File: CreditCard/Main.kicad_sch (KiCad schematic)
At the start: 0 parts

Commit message: début
début sch
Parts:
- added C10, C11, C18, C19, C20, C21: 0.1uF, Capacitor_SMD:C_0603_1608Metric, symbol Device:C
- added SW1, SW2, SW3: 2425754-1, Library:2425754-1_TEC, symbol LIB:2425754-1
- added U5, U6, U7: PTS645SK43SMTR92LFS, Library:SWITCH_45SK43SMTR92LFS, symbol Library:PTS645SK43SMTR92LFS
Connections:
- new net GND: C10.2, C11.2, C18.2, C19.2, C20.2, C21.2, SW1.2, SW1.3, SW2.2, SW2.3, SW3.2, SW3.3, U5.3, U5.4, U6.3, U6.4, U7.3, U7.4
- new net GPIO2: C10.1, SW1.1, SW1.4
- new net GPIO3: C11.1, SW2.1, SW2.4
- new net GPIO4: C18.1, SW3.1, SW3.4
- new net GPIO5: C19.1, U5.1, U5.2
- new net GPIO6: C20.1, U6.1, U6.2
- new net GPIO7: C21.1, U7.1, U7.2
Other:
- note added: "JEUX"
- note added: "MENU"

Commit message: manque écran
manque seulement l'écran le reste est ajouter
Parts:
- added U10: PAM8403DR, Library:SOIC_8403DR_DIO, symbol Library:PAM8403DR
- added U9: SPKM.36.8.B, Library:SPEAKER, symbol Library:SPEAKER
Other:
- note added: "SPEAKER"
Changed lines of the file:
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@@
 		)
 	)
+	(rectangle
+		(start 129.54 15.24)
+		(end 241.3 93.98)
+		(stroke
+			(width 0.381)
+			(type dash)
+			(color 20 0 0 1)
+		)
+		(fill
+			(type none)
+		)
+	)
 	(text "JEUX\n"
 		(exclude_from_sim no)
@@
 		)
 	)
+	(text "SPEAKER\n"
+		(exclude_from_sim no)
+		(at 138.43 19.812 0)
+		(effects
+			(font
+				(size 2.286 2.286)
+				(thickness 0.4064)
+				(bold yes)
+			)
+		)
+	)
 	(text "MENU"
 		(exclude_from_sim no)
@@
 	)
 	(symbol
+		(lib_id "Library:SPEAKER")
+		(at 214.63 48.26 0)
+		(unit 1)
+		(exclude_from_sim no)
+		(in_bom yes)
+		(on_board yes)
+		(dnp no)
+		(fields_autoplaced yes)
+		(property "Reference" "U9"
+			(at 219.075 41.91 0)
+			(effects
+				(font
+					(size 1.27 1.27)
+				)
+			)
+		)
+		(property "Value" "SPKM.36.8.B"
+			(at 219.075 44.45 0)
+			(effects
+				(font
+					(size 1.27 1.27)
+				)
+			)
+		)
+		(property "Footprint" "Library:SPEAKER"
+			(at 214.63 48.26 0)
+			(effects
+				(font
+					(size 1.27 1.27)
+				)
+				(hide yes)
+			)
+		)
+		(property "Datasheet" "https://www.taoglas.com/datasheets/SPKM.36.8.B.pdf"
+			(at 214.63 48.26 0)
+			(effects
+				(font
+					(size 1.27 1.27)
+				)
+				(hide yes)
+			)
+		)
+		(property "Description" ""
+			(at 214.63 48.26 0)
+			(effects
+				(font
+					(size 1.27 1.27)
+				)
+				(hide yes)
+			)
+		)
+		(pin "2"
+		)
+		(pin "1"
+		)
+		(instances
+			(project ""
+				(path "/374dba13-75d6-44a0-b8b2-0ca0aa70330e/712f9979-8db9-4af3-ac95-adf708c06b03"
+					(reference "U9")
+					(unit 1)
+				)
+			)
+		)
+	)
+	(symbol
 		(lib_id "Device:C")
 		(at 74.93 53.34 0)
@@
 					(unit 1)
 				)
+			)
+		)
+	)
+	(symbol
+		(lib_id "Library:PAM8403DR")
+		(at 137.16 44.45 0)
+		(unit 1)
+		(exclude_from_sim no)
+		(in_bom yes)
+		(on_board yes)
+		(dnp no)
+		(fields_autoplaced yes)
+		(property "Reference" "U10"
+			(at 162.56 34.29 0)
+			(effects
+				(font
+					(size 1.524 1.524)
+				)
+			)
+		)
+		(property "Value" "PAM8403DR"
+			(at 162.56 36.83 0)
+			(effects
+				(font
+					(size 1.524 1.524)
+				)
+			)
+		)
+		(property "Footprint" "Library:SOIC_8403DR_DIO"
+			(at 137.16 44.45 0)
+			(effects
+				(font
+					(size 1.27 1.27)
+					(italic yes)
+				)
+				(hide yes)
+			)
+		)
+		(property "Datasheet" "PAM8403DR"
+			(at 137.16 44.45 0)
+			(effects
+				(font
+					(size 1.27 1.27)
+					(italic yes)
+				)
+				(hide yes)
+			)
+		)
+		(property "Description" ""
+			(at 137.16 44.45 0)
+			(effects
+				(font
+					(size 1.27 1.27)
+				)
+				(hide yes)
+			)
+		)
+		(pin "1"
+		)
+		(pin "3"
+		)
+		(pin "2"
+		)
+		(pin "7"
+		)
+		(pin "8"
+		)
+		(pin "4"
+		)
+		(pin "16"
+		)
+		(pin "13"
+		)
+		(pin "11"
+		)
+		(pin "6"
+		)
+		(pin "14"
+		)
+		(pin "10"
+		)
+		(pin "12"
+		)
+		(pin "5"
+		)
+		(pin "15"
+		)
+		(pin "9"
+		)
+		(instances
+			(project ""
+				(path "/374dba13-75d6-44a0-b8b2-0ca0aa70330e/712f9979-8db9-4af3-ac95-adf708c06b03"
+					(reference "U10")
+					(unit 1)
+				)

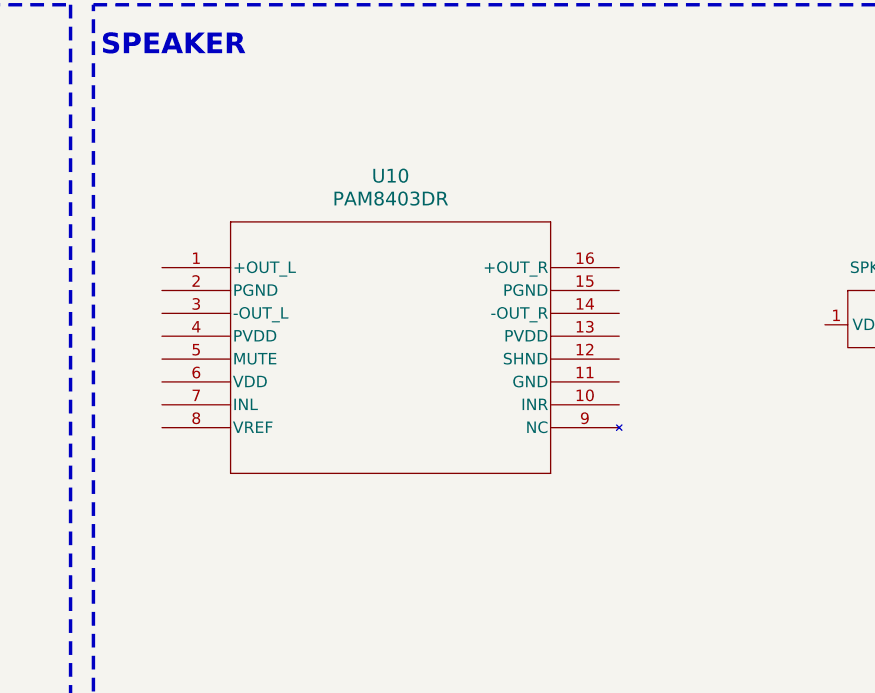
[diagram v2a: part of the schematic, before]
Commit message: ajout des gold fingers
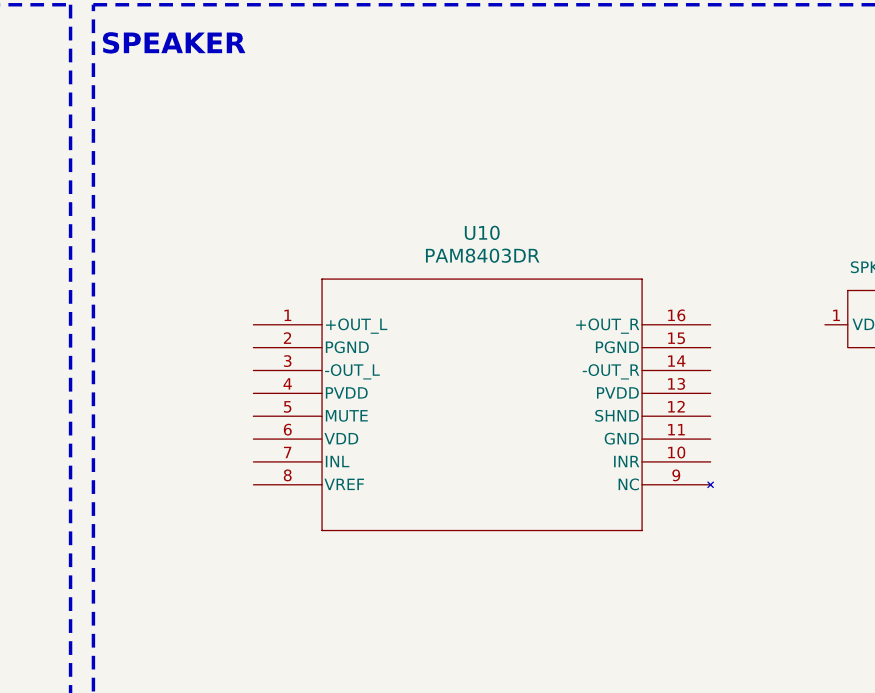
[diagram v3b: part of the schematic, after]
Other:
- moved on the sheet: U10
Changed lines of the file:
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@@
 	(symbol
 		(lib_id "Library:PAM8403DR")
-		(at 137.16 44.45 0)
+		(at 147.32 50.8 0)
 		(unit 1)
 		(exclude_from_sim no)
@@
 		(fields_autoplaced yes)
 		(property "Reference" "U10"
-			(at 162.56 34.29 0)
+			(at 172.72 40.64 0)
 			(effects
 				(font
@@
 		)
 		(property "Value" "PAM8403DR"
-			(at 162.56 36.83 0)
+			(at 172.72 43.18 0)
 			(effects
 				(font
@@
 		)
 		(property "Footprint" "Library:SOIC_8403DR_DIO"
-			(at 137.16 44.45 0)
+			(at 147.32 50.8 0)
 			(effects
 				(font
@@
 		)
 		(property "Datasheet" "PAM8403DR"
-			(at 137.16 44.45 0)
+			(at 147.32 50.8 0)
 			(effects
 				(font
@@
 		)
 		(property "Description" ""
-			(at 137.16 44.45 0)
+			(at 147.32 50.8 0)
 			(effects
 				(font

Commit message: debut Alice
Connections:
- net GND: now also U10.11 (GND), U10.15 (PGND), U10.2 (PGND), U10.9 (NC)
- net at U9.1 (VDD): now also U10.16 (+OUT_R)
- net at U9.2 (GND): now also U10.14 (-OUT_R)
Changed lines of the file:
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@@
 	)
 	(junction
+		(at 205.74 63.5)
+		(diameter 0)
+		(color 0 0 0 0)
+	)
+	(junction
 		(at 86.36 137.16)
 		(diameter 0)
@@
 	)
 	(junction
+		(at 205.74 68.58)
+		(diameter 0)
+		(color 0 0 0 0)
+	)
+	(junction
 		(at 86.36 153.67)
 		(diameter 0)
@@
 	(wire
 		(pts
+			(xy 198.12 53.34) (xy 205.74 53.34)
+		)
+		(stroke
+			(width 0)
+			(type default)
+		)
+	)
+	(wire
+		(pts
 			(xy 66.04 66.04) (xy 74.93 66.04)
 		)
@@
 	(wire
 		(pts
+			(xy 198.12 63.5) (xy 205.74 63.5)
+		)
+		(stroke
+			(width 0)
+			(type default)
+		)
+	)
+	(wire
+		(pts
 			(xy 74.93 41.91) (xy 74.93 40.64)
 		)
@@
 	(wire
 		(pts
+			(xy 147.32 53.34) (xy 138.43 53.34)
+		)
+		(stroke
+			(width 0)
+			(type default)
+		)
+	)
+	(wire
+		(pts
+			(xy 198.12 50.8) (xy 210.82 50.8)
+		)
+		(stroke
+			(width 0)
+			(type default)
+		)
+	)
+	(wire
+		(pts
+			(xy 227.33 50.8) (xy 227.33 55.88)
+		)
+		(stroke
+			(width 0)
+			(type default)
+		)
+	)
+	(wire
+		(pts
 			(xy 77.47 137.16) (xy 86.36 137.16)
 		)
@@
 	(wire
 		(pts
+			(xy 138.43 53.34) (xy 138.43 74.93)
+		)
+		(stroke
+			(width 0)
+			(type default)
+		)
+	)
+	(wire
+		(pts
 			(xy 83.82 66.04) (xy 74.93 66.04)
 		)
@@
 	(wire
 		(pts
+			(xy 205.74 53.34) (xy 205.74 63.5)
+		)
+		(stroke
+			(width 0)
+			(type default)
+		)
+	)
+	(wire
+		(pts
+			(xy 205.74 68.58) (xy 205.74 77.47)
+		)
+		(stroke
+			(width 0)
+			(type default)
+		)
+	)
+	(wire
+		(pts
 			(xy 77.47 177.8) (xy 86.36 177.8)
 		)
@@
 	(wire
 		(pts
+			(xy 198.12 68.58) (xy 205.74 68.58)
+		)
+		(stroke
+			(width 0)
+			(type default)
+		)
+	)
+	(wire
+		(pts
 			(xy 74.93 58.42) (xy 74.93 57.15)
 		)
@@
 	(wire
 		(pts
+			(xy 205.74 63.5) (xy 205.74 68.58)
+		)
+		(stroke
+			(width 0)
+			(type default)
+		)
+	)
+	(wire
+		(pts
 			(xy 83.82 33.02) (xy 74.93 33.02)
 		)
@@
 	(wire
 		(pts
+			(xy 227.33 55.88) (xy 198.12 55.88)
+		)
+		(stroke
+			(width 0)
+			(type default)
+		)
+	)
+	(wire
+		(pts
 			(xy 74.93 74.93) (xy 74.93 73.66)
 		)
@@
 	(symbol
 		(lib_id "power:GND")
+		(at 138.43 74.93 0)
+		(unit 1)
+		(exclude_from_sim no)
+		(in_bom yes)
+		(on_board yes)
+		(dnp no)
+		(fields_autoplaced yes)
+		(property "Reference" "#PWR061"
+			(at 138.43 81.28 0)
+			(effects
+				(font
+					(size 1.27 1.27)
+				)
+				(hide yes)
+			)
+		)
+		(property "Value" "GND"
+			(at 138.43 80.01 0)
+			(effects
+				(font
+					(size 1.27 1.27)
+				)
+			)
+		)
+		(property "Footprint" ""
+			(at 138.43 74.93 0)
+			(effects
+				(font
+					(size 1.27 1.27)
+				)
+				(hide yes)
+			)
+		)
+		(property "Datasheet" ""
+			(at 138.43 74.93 0)
+			(effects
+				(font
+					(size 1.27 1.27)
+				)
+				(hide yes)
+			)
+		)
+		(property "Description" "Power symbol creates a global label with name \"GND\" , ground"
+			(at 138.43 74.93 0)
+			(effects
+				(font
+					(size 1.27 1.27)
+				)
+				(hide yes)
+			)
+		)
+		(pin "1"
+		)
+		(instances
+			(project "CreditCard"
+				(path "/374dba13-75d6-44a0-b8b2-0ca0aa70330e/712f9979-8db9-4af3-ac95-adf708c06b03"
+					(reference "#PWR061")
+					(unit 1)
+				)
+			)
+		)
+	)
+	(symbol
+		(lib_id "power:GND")
 		(at 43.18 71.12 0)
 		(unit 1)
@@
 	)
 	(symbol
+		(lib_id "power:GND")
+		(at 205.74 77.47 0)
+		(unit 1)
+		(exclude_from_sim no)
+		(in_bom yes)
+		(on_board yes)
+		(dnp no)
+		(fields_autoplaced yes)
+		(property "Reference" "#PWR053"
+			(at 205.74 83.82 0)
+			(effects
+				(font
+					(size 1.27 1.27)
+				)
+				(hide yes)
+			)
+		)
+		(property "Value" "GND"
+			(at 205.74 82.55 0)
+			(effects
+				(font
+					(size 1.27 1.27)
+				)
+			)
+		)
+		(property "Footprint" ""
+			(at 205.74 77.47 0)
+			(effects
+				(font
+					(size 1.27 1.27)
+				)
+				(hide yes)
+			)
+		)
+		(property "Datasheet" ""
+			(at 205.74 77.47 0)
+			(effects
+				(font
+					(size 1.27 1.27)
+				)
+				(hide yes)
+			)
+		)
+		(property "Description" "Power symbol creates a global label with name \"GND\" , ground"
+			(at 205.74 77.47 0)
+			(effects
+				(font
+					(size 1.27 1.27)
+				)
+				(hide yes)
+			)
+		)
+		(pin "1"
+		)
+		(instances
+			(project ""
+				(path "/374dba13-75d6-44a0-b8b2-0ca0aa70330e/712f9979-8db9-4af3-ac95-adf708c06b03"
+					(reference "#PWR053")
+					(unit 1)
+				)
+			)
+		)
+	)
+	(symbol
 		(lib_id "Library:PAM8403DR")
 		(at 147.32 50.8 0)
@@
 			)
 		)
-		(property "Datasheet" "PAM8403DR"
+		(property "Datasheet" "https://www.diodes.com/assets/Datasheets/products_inactive_data/PAM8403.pdf"
 			(at 147.32 50.8 0)
 			(effects

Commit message: connection du audio amp
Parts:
- added C22, C6: 4.7uF, Capacitor_SMD:C_0603_1608Metric, symbol Device:C
- added C23, C26, C5: 0.1uF, Capacitor_SMD:C_0603_1608Metric, symbol Device:C
- added C24: 470uf, Capacitor_SMD:C_0603_1608Metric, symbol Device:C
- added C25: 1uf, Capacitor_SMD:C_0603_1608Metric, symbol Device:C
- added R15, R16: 18k, Resistor_SMD:R_0603_1608Metric, symbol Device:R_US
- added R18: 0, Resistor_SMD:R_0603_1608Metric, symbol Device:R_US
- added U11: SPKM.36.8.B, Library:SPEAKER, symbol Library:SPEAKER
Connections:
- net GND: now also C23.2, C24.2, C25.2, C26.1, C5.2
- net at U10.1 (+OUT_L): now also U11.1 (VDD)
- net at U10.10 (INR): now also R16.2
- net AudioCS: now reaches U10.12 (SHND)
- net 3V3: now reaches U10.13 (PVDD)
- net 3V3: now also U10.4 (PVDD), U10.6 (VDD), C23.1, C24.1, C25.1, C26.2, R18.1
- net at U10.3 (-OUT_L): now also U11.2 (GND)
- net at U10.5 (MUTE): now also R18.2
- net at U10.7 (INL): now also R15.1
- net at U10.8 (VREF): now also C5.1
- new net: C22.1, R16.1
- new net: C6.1, R15.2
- new net AudioL: C6.2
- new net AudioR: C22.2
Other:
- moved on the sheet: C21, U10, U7, U9

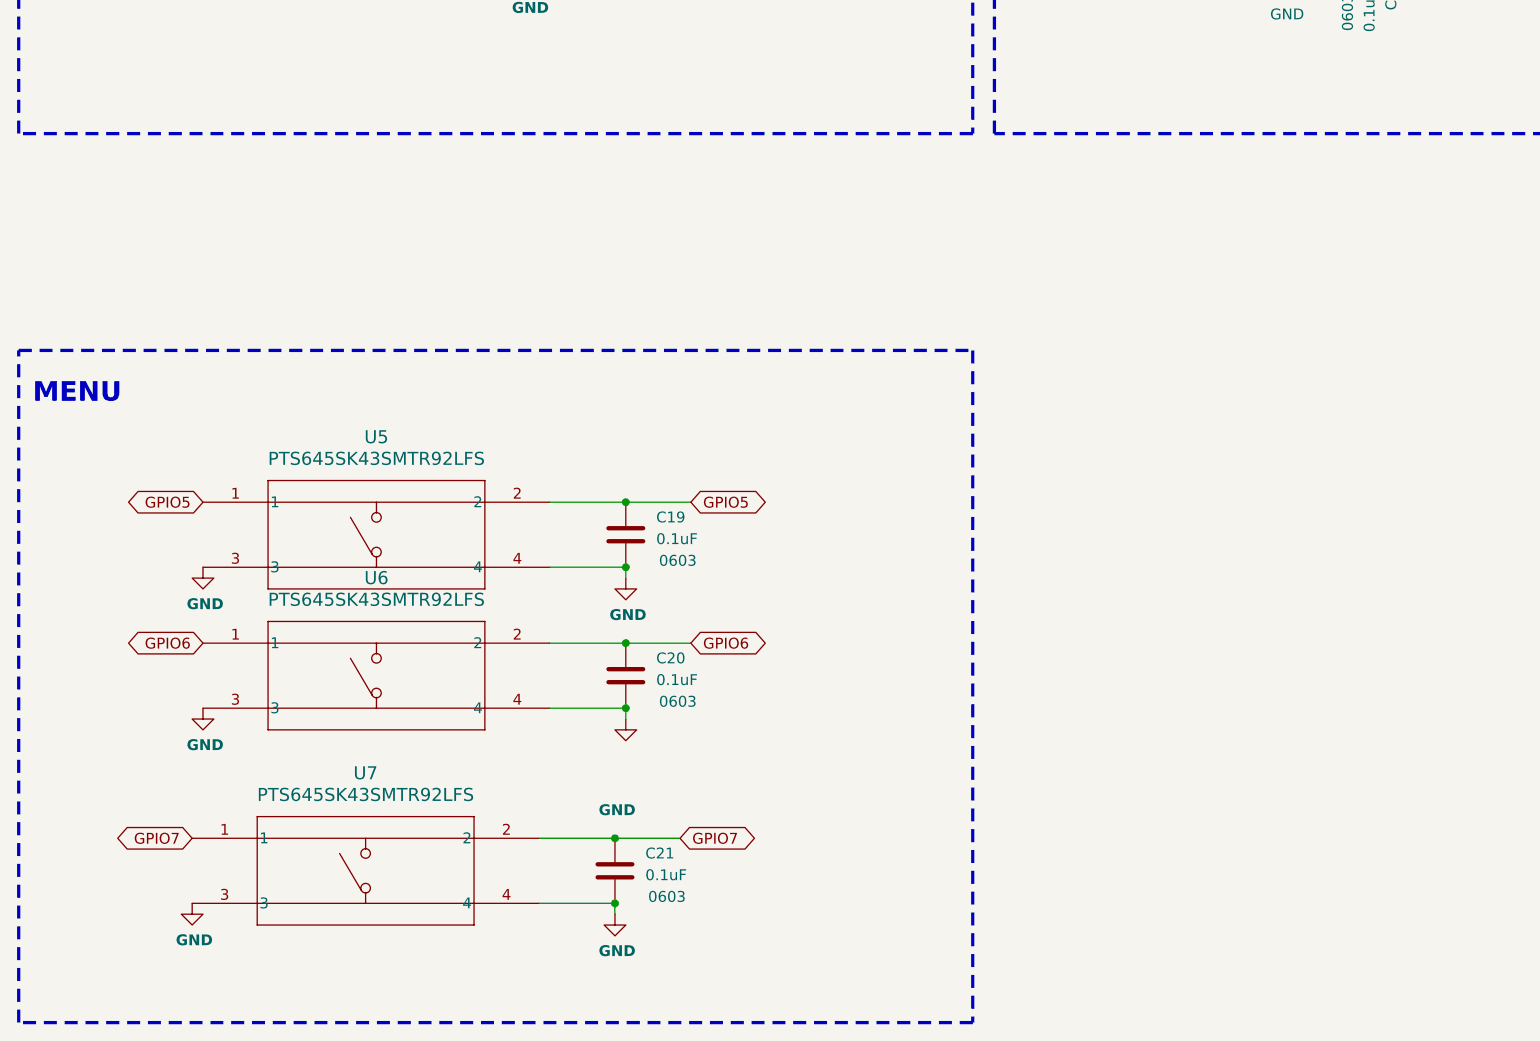
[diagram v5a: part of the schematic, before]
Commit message: ajout du LCD
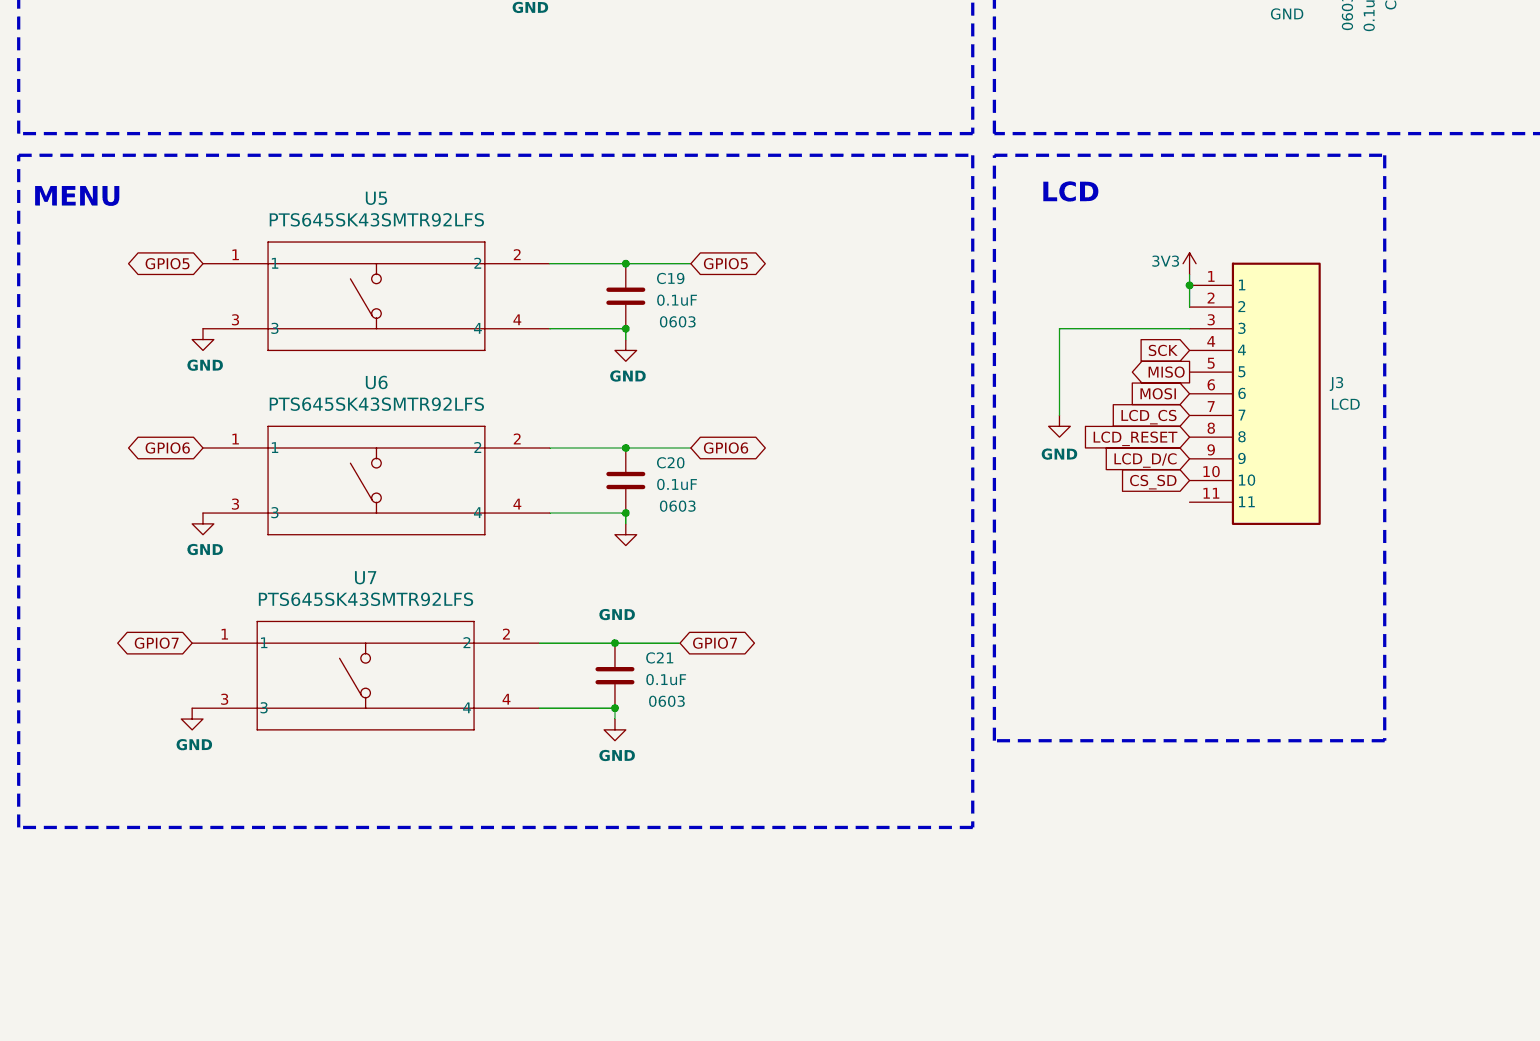
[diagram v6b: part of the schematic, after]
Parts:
- added J3: LCD, Library:LCD, symbol Library:LCD
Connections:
- net 3V3: now also J3.1, J3.2
- net GND: now also J3.3
- new net CS_SD: J3.10
- new net LCD_CS: J3.7
- new net LCD_D/C: J3.9
- new net LCD_RESET: J3.8
- new net MISO: J3.5
- new net MOSI: J3.6
- new net SCK: J3.4
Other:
- note added: "LCD"
- moved on the sheet: C19, C20, C21, U5, U6, U7

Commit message: aliiice
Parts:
- removed J3: LCD, Library:LCD, symbol Library:LCD
- added J2: LCD, Library:LCD, symbol Library:LCD
- added R19, R21: 0, Resistor_SMD:R_0603_1608Metric, symbol Device:R_US
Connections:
- net 3V3: now also J2.1, R19.2
- net CS_SD: now also J2.10
- net GND: now also J2.3, R21.1
- net LCD_CS: now also J2.7
- net LCD_D/C: now also J2.9
- net LCD_RESET: now also J2.8
- net MISO: now also J2.5
- net MOSI: now also J2.6
- net SCK: now also J2.4
- new net: J2.11, R19.1, R21.2

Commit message: petite retouche et bom complet
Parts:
- added C27, C28, C29, C30, C31, C32, C33, C34, C35, C36: 0.1uF, Capacitor_SMD:C_0603_1608Metric, symbol Device:C
- C24: now not fitted; now left out of the parts list
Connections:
- net 3V3: now also C27.1, C28.1, C29.1, C30.1, C31.1, C32.1, C33.1, C34.1, C35.1, C36.1; no longer C24.1
- net GND: now also C27.2, C28.2, C29.2, C30.2, C31.2, C32.2, C33.2, C34.2, C35.2, C36.2; no longer C24.2
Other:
- note added: "TROP GROSSE CAP change pour 10 plus petite en para"
- moved on the sheet: C23, C25, U11, U9
